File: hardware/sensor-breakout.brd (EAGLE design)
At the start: 44 x 44 mm, 67 parts, among them IC1 ATMEGA168-MU, U1 MCP73831, U2 NRF24L01SMD, U4 MCP5301, Y1 16M, Y2 12MHz

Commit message: hw: rc1
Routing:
- net GND: vias 38 -> 58
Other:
- board text added: "+3V3"
- board text added: "GND"
- board text added: "PC0"
- board text added: "PC1"
- board text added: "PC2"
- board text added: "PC3"
- board text added: "PD0"
- board text added: "PD3"
- board text added: "PD4"
- board text added: "SCL"
- board text added: "SDA"
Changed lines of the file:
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@@
 <rectangle x1="41.275" y1="1.905" x2="42.545" y2="3.175" layer="30"/>
 <rectangle x1="38.735" y1="1.905" x2="40.005" y2="3.175" layer="30"/>
+<text x="22.7584" y="5.08" size="0.6096" layer="121" rot="R90" align="center">PC0</text>
+<text x="22.7584" y="2.6416" size="0.6096" layer="121" rot="R90" align="center">+3V3</text>
+<text x="22.7584" y="7.7216" size="0.6096" layer="121" rot="R90" align="center">PC1</text>
+<text x="22.7584" y="10.16" size="0.6096" layer="121" rot="R90" align="center">PC2</text>
+<text x="22.7584" y="12.5984" size="0.6096" layer="121" rot="R90" align="center">PC3</text>
+<text x="22.7584" y="15.24" size="0.6096" layer="121" rot="R90" align="center">SDA</text>
+<text x="22.7584" y="17.8816" size="0.6096" layer="121" rot="R90" align="center">SCL</text>
+<text x="22.7584" y="20.32" size="0.6096" layer="121" rot="R90" align="center">PD0</text>
+<text x="22.7584" y="22.9616" size="0.6096" layer="121" rot="R90" align="center">PD3</text>
+<text x="22.7584" y="25.4" size="0.6096" layer="121" rot="R90" align="center">PD4</text>
+<text x="22.7584" y="35.56" size="0.6096" layer="121" rot="R90" align="center">GND</text>
 </plain>
 <attributes>
@@
 <via x="21.1328" y="0.8128" extent="1-16" drill="0.381"/>
 <wire x1="16.4592" y1="11.3792" x2="16.4592" y2="12.192" width="0" layer="19" extent="1-1"/>
+<via x="8.9408" y="7.9248" extent="1-16" drill="0.381"/>
+<via x="8.128" y="7.9248" extent="1-16" drill="0.381"/>
+<via x="8.3312" y="0.8128" extent="1-16" drill="0.381"/>
+<via x="18.0848" y="6.096" extent="1-16" drill="0.381"/>
+<via x="12.192" y="7.5184" extent="1-16" drill="0.381"/>
+<via x="14.8336" y="7.5184" extent="1-16" drill="0.381"/>
+<via x="0.8128" y="14.6304" extent="1-16" drill="0.381"/>
+<via x="4.064" y="15.6464" extent="1-16" drill="0.381"/>
+<via x="3.8608" y="26.8224" extent="1-16" drill="0.381"/>
+<via x="5.2832" y="26.8224" extent="1-16" drill="0.381"/>
+<via x="3.8608" y="24.5872" extent="1-16" drill="0.381"/>
+<via x="5.2832" y="24.5872" extent="1-16" drill="0.381"/>
+<via x="6.096" y="25.6032" extent="1-16" drill="0.381"/>
+<via x="15.24" y="23.368" extent="1-16" drill="0.381"/>
+<via x="19.9136" y="20.5232" extent="1-16" drill="0.381"/>
+<via x="19.5072" y="18.288" extent="1-16" drill="0.381"/>
+<via x="20.7264" y="17.0688" extent="1-16" drill="0.381"/>
+<via x="9.144" y="18.288" extent="1-16" drill="0.381"/>
+<via x="6.096" y="15.8496" extent="1-16" drill="0.381"/>
+<via x="8.128" y="16.8656" extent="1-16" drill="0.381"/>
 </signal>
 <signal name="+5V">
@@
 <via x="15.24" y="15.6464" extent="1-16" drill="0.381"/>
 <wire x1="15.24" y1="15.6464" x2="14.0208" y2="14.4272" width="0.2032" layer="16"/>
-<wire x1="14.0208" y1="14.4272" x2="14.0208" y2="10.9728" width="0.2032" layer="16"/>
-<wire x1="14.0208" y1="10.9728" x2="15.6464" y2="9.3472" width="0.2032" layer="16"/>
-<wire x1="15.6464" y1="9.3472" x2="15.6464" y2="6.9088" width="0.2032" layer="16"/>
+<wire x1="14.0208" y1="14.4272" x2="14.0208" y2="10.3632" width="0.2032" layer="16"/>
+<wire x1="14.0208" y1="10.3632" x2="15.6464" y2="8.7376" width="0.2032" layer="16"/>
+<wire x1="15.6464" y1="8.7376" x2="15.6464" y2="6.9088" width="0.2032" layer="16"/>
 <wire x1="15.6464" y1="6.9088" x2="17.4752" y2="5.08" width="0.2032" layer="16"/>
 <via x="17.4752" y="5.08" extent="1-16" drill="0.381"/>

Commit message: hw: rc2
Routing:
- net GND: vias 58 -> 59
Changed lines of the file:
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@@
 <setting verticaltext="up"/>
 </settings>
-<grid distance="8" unitdist="mil" unit="mil" style="lines" multiple="1" display="yes" altdistance="5" altunitdist="mil" altunit="mil"/>
+<grid distance="25" unitdist="mil" unit="mil" style="lines" multiple="1" display="yes" altdistance="5" altunitdist="mil" altunit="mil"/>
 <layers>
 <layer number="1" name="Top" color="4" fill="1" visible="yes" active="yes"/>
@@
 <text x="22.7584" y="25.4" size="0.6096" layer="121" rot="R90" align="center">PD4</text>
 <text x="22.7584" y="35.56" size="0.6096" layer="121" rot="R90" align="center">GND</text>
+<rectangle x1="36.195" y1="34.925" x2="37.465" y2="36.195" layer="29"/>
+<rectangle x1="38.735" y1="34.925" x2="40.005" y2="36.195" layer="29"/>
+<rectangle x1="41.275" y1="34.925" x2="42.545" y2="36.195" layer="29"/>
+<rectangle x1="36.195" y1="34.925" x2="37.465" y2="36.195" layer="30"/>
+<rectangle x1="38.735" y1="34.925" x2="40.005" y2="36.195" layer="30"/>
+<rectangle x1="41.275" y1="34.925" x2="42.545" y2="36.195" layer="30"/>
 </plain>
 <attributes>
@@
 <via x="31.75" y="35.56" extent="1-16" drill="1.016" diameter="1.8796"/>
 <via x="34.29" y="35.56" extent="1-16" drill="1.016" diameter="1.8796"/>
-<via x="36.83" y="35.56" extent="1-16" drill="1.016" diameter="1.8796"/>
-<via x="39.37" y="35.56" extent="1-16" drill="1.016" diameter="1.8796"/>
 <wire x1="20.7636" y1="15.8496" x2="20.7636" y2="15.406" width="0.6096" layer="1"/>
 <wire x1="20.7636" y1="15.406" x2="20.9296" y2="15.24" width="0.6096" layer="1"/>
 <wire x1="20.9296" y1="15.24" x2="20.9296" y2="14.6676" width="0.6096" layer="1"/>
 <wire x1="20.9296" y1="14.6676" x2="20.9668" y2="14.6304" width="0.6096" layer="1"/>
-<via x="41.91" y="35.56" extent="1-16" drill="1.016" diameter="1.8796"/>
 <via x="21.1328" y="0.8128" extent="1-16" drill="0.381"/>
-<wire x1="16.4592" y1="11.3792" x2="16.4592" y2="12.192" width="0" layer="19" extent="1-1"/>
 <via x="8.9408" y="7.9248" extent="1-16" drill="0.381"/>
 <via x="8.128" y="7.9248" extent="1-16" drill="0.381"/>
@@
 <via x="6.096" y="15.8496" extent="1-16" drill="0.381"/>
 <via x="8.128" y="16.8656" extent="1-16" drill="0.381"/>
+<via x="38.1" y="36.195" extent="1-16" drill="0.381"/>
+<via x="40.64" y="36.195" extent="1-16" drill="0.381"/>
+<via x="43.18" y="36.195" extent="1-16" drill="0.381"/>
+<via x="43.18" y="34.925" extent="1-16" drill="0.381"/>
+<wire x1="16.4592" y1="11.3792" x2="16.4592" y2="12.192" width="0" layer="19" extent="1-1"/>
 </signal>
 <signal name="+5V">

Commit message: hw: update values
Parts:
- R1: value TBD -> 3k9
- R2: value 2k2 -> 1k5
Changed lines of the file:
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@@
 <element name="C8" library="rcl" package="C0603" value="33p" x="18.288" y="20.32" rot="MR90"/>
 <element name="C9" library="rcl" package="C0603" value="33p" x="16.8656" y="20.32" rot="MR90"/>
-<element name="R2" library="rcl" package="R0603" value="2k2" x="7.3152" y="20.5232"/>
+<element name="R2" library="rcl" package="R0603" value="1k5" x="7.3152" y="20.5232"/>
 <element name="R3" library="rcl" package="R0603" value="68" x="6.2992" y="18.8976" rot="MR90"/>
 <element name="R4" library="rcl" package="R0603" value="68" x="7.7216" y="18.8976" rot="MR90"/>
@@
 <attribute name="PROD_ID" value="IC-09995" x="2.4384" y="12.5984" size="1.778" layer="27" rot="R270" display="off"/>
 </element>
-<element name="R1" library="rcl" package="R0603" value="TBD" x="3.6576" y="12.5984" rot="MR270"/>
+<element name="R1" library="rcl" package="R0603" value="3k9" x="3.6576" y="12.5984" rot="MR270"/>
 <element name="R5" library="rcl" package="R0603" value="5k6" x="7.9248" y="3.2512" rot="R270"/>
 <element name="R6" library="rcl" package="R0603" value="5k6" x="21.7424" y="3.8608" rot="R90"/>

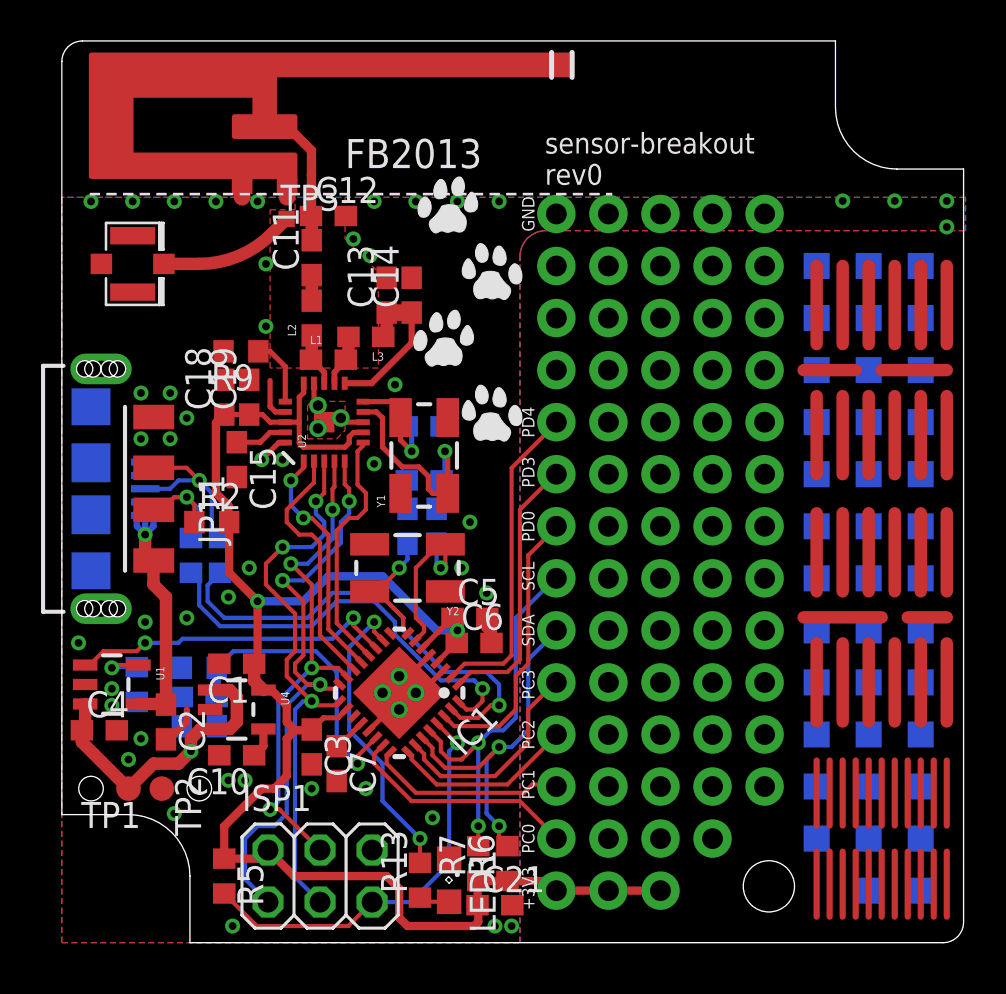
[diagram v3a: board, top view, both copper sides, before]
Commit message: hw: rev1, moved battery pads on bottom
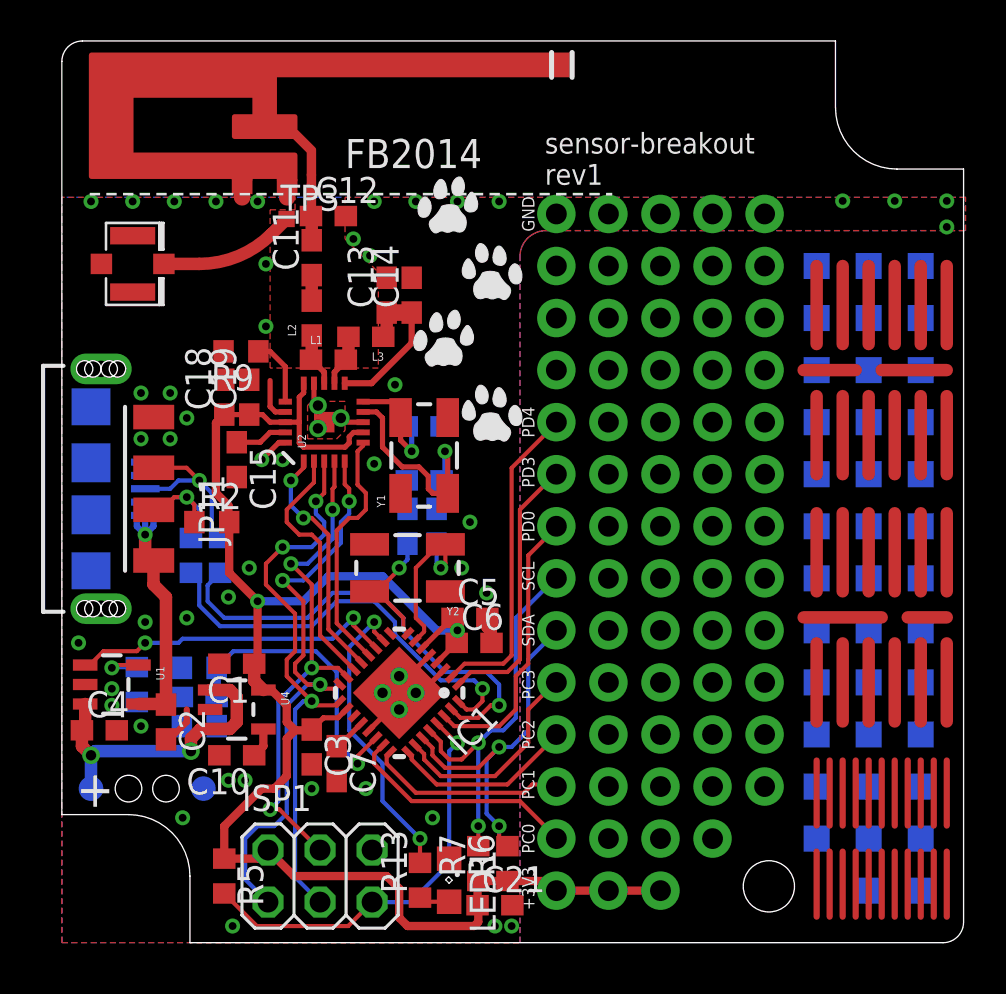
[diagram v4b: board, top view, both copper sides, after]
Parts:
- moved TP2 2.03 mm to (6.91, 7.52), flipped to the bottom
- moved TP1 1.83 mm to (1.42, 7.52), flipped to the bottom
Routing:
- net VBATT: track 16.2 -> 16.6 mm, vias 1 -> 2
- net GND: vias 59 -> 58
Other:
- board text added: "+"
- board text added: "FB2014"
- board text added: "sensor-breakout rev1"
- board text removed: "FB2013"
- board text removed: "sensor-breakout rev0"
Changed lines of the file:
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@@
 <setting verticaltext="up"/>
 </settings>
-<grid distance="25" unitdist="mil" unit="mil" style="lines" multiple="1" display="yes" altdistance="5" altunitdist="mil" altunit="mil"/>
+<grid distance="8" unitdist="mil" unit="mil" style="lines" multiple="1" display="yes" altdistance="5" altunitdist="mil" altunit="mil"/>
 <layers>
 <layer number="1" name="Top" color="4" fill="1" visible="yes" active="yes"/>
@@
 <board>
 <plain>
-<hole x="6.7056" y="7.5184" drill="1.2"/>
-<hole x="1.4224" y="7.5184" drill="1.2"/>
-<text x="13.8176" y="37.7952" size="1.4224" layer="121">FB2013</text>
+<hole x="5.08" y="7.5184" drill="1.3"/>
+<hole x="3.2512" y="7.5184" drill="1.3"/>
+<text x="13.8176" y="37.7952" size="1.4224" layer="121">FB2014</text>
 <text x="23.5712" y="36.9824" size="1.016" layer="121">sensor-breakout
-rev0</text>
+rev1</text>
 <rectangle x1="11.9888" y1="24.6888" x2="13.6144" y2="26.3144" layer="29"/>
 <wire x1="-5" y1="22" x2="49" y2="22" width="0.4064" layer="47"/>
@@
 <rectangle x1="38.735" y1="34.925" x2="40.005" y2="36.195" layer="30"/>
 <rectangle x1="41.275" y1="34.925" x2="42.545" y2="36.195" layer="30"/>
+<text x="1.6256" y="7.5184" size="1.778" layer="121" align="center">+</text>
 </plain>
 <attributes>
@@
 </element>
 <element name="U$1" library="antenna" package="DN007-2" value="INVERTED_F_ANTENNA-2" x="9.9568" y="39.8272"/>
-<element name="TP1" library="testpad" package="TP12R" value="TPTP12R" x="3.2512" y="7.5184" rot="R180">
-<attribute name="TP_SIGNAL_NAME" value="" x="-13.2588" y="63.3984" size="1.778" layer="27" rot="R180" display="off"/>
+<element name="TP1" library="testpad" package="TP12R" value="TPTP12R" x="1.4224" y="7.5184" rot="MR180">
+<attribute name="TP_SIGNAL_NAME" value="" x="17.9324" y="63.3984" size="1.778" layer="28" rot="MR180" display="off"/>
 </element>
-<element name="TP2" library="testpad" package="TP12R" value="TPTP12R" x="4.8768" y="7.5184" rot="R270">
-<attribute name="TP_SIGNAL_NAME" value="" x="-51.0032" y="-14.0716" size="1.778" layer="27" rot="R270" display="off"/>
+<element name="TP2" library="testpad" package="TP12R" value="TPTP12R" x="6.9088" y="7.5184" rot="MR270">
+<attribute name="TP_SIGNAL_NAME" value="" x="62.7888" y="-14.0716" size="1.778" layer="28" rot="MR270" display="off"/>
 </element>
 <element name="U$2" library="SparkFun-Connectors" package="U.FL" value="U.FL" x="3.4544" y="33.1216"/>
@@
 <via x="2.4384" y="12.3952" extent="1-16" drill="0.381"/>
 <via x="2.4384" y="11.5824" extent="1-16" drill="0.381"/>
-<via x="3.2512" y="8.9408" extent="1-16" drill="0.381"/>
-<via x="3.8608" y="9.9568" extent="1-16" drill="0.381"/>
+<via x="3.8608" y="10.5664" extent="1-16" drill="0.381"/>
 <wire x1="14.974275" y1="10.353521875" x2="15.999953125" y2="11.3792" width="0.254" layer="1"/>
 <wire x1="15.999953125" y1="11.3792" x2="16.4592" y2="11.3792" width="0.254" layer="1"/>
@@
 <wire x1="6.096" y1="10.7696" x2="5.2832" y2="9.9568" width="0.3048" layer="1"/>
 <wire x1="5.2832" y1="9.9568" x2="4.8768" y2="9.9568" width="0.3048" layer="1"/>
-<via x="5.4864" y="6.2992" extent="1-16" drill="0.381"/>
+<via x="5.8928" y="6.096" extent="1-16" drill="0.381"/>
 <via x="10.7696" y="23.5712" extent="1-16" drill="0.381"/>
 <via x="9.7536" y="23.5712" extent="1-16" drill="0.381"/>
@@
 <wire x1="1.1383" y1="11.6484" x2="1.1383" y2="10.5227" width="0.6096" layer="1"/>
 <wire x1="1.1383" y1="10.5227" x2="0.9788" y2="10.3632" width="0.6096" layer="1"/>
-<wire x1="0.9788" y1="10.3632" x2="0.9788" y2="9.7908" width="0.6096" layer="1"/>
-<wire x1="0.9788" y1="9.7908" x2="3.2512" y2="7.5184" width="0.6096" layer="1"/>
-<wire x1="3.2512" y1="7.5184" x2="4.4704" y2="8.7376" width="0.6096" layer="1"/>
-<wire x1="4.4704" y1="8.7376" x2="5.6896" y2="8.7376" width="0.6096" layer="1"/>
-<wire x1="5.6896" y1="8.7376" x2="6.2992" y2="9.3472" width="0.6096" layer="1"/>
 <wire x1="6.2992" y1="9.9568" x2="6.7716" y2="10.4292" width="0.6096" layer="1"/>
 <wire x1="7.2343" y1="10.4292" x2="6.7716" y2="10.4292" width="0.6096" layer="1"/>
@@
 <wire x1="8.194" y1="12.3292" x2="8.5344" y2="11.9888" width="0.6096" layer="1"/>
 <wire x1="6.2992" y1="9.3472" x2="6.2992" y2="9.9568" width="0.6096" layer="1"/>
-<via x="6.2992" y="9.3472" extent="1-16" drill="0.381"/>
+<via x="6.2992" y="9.3472" extent="1-16" drill="0.508"/>
 <wire x1="6.2992" y1="9.3472" x2="6.2992" y2="10.1228" width="0.4064" layer="16"/>
 <wire x1="6.2992" y1="10.1228" x2="5.8556" y2="10.5664" width="0.4064" layer="16"/>
+<wire x1="0.9788" y1="10.3632" x2="0.9788" y2="9.5876" width="0.6096" layer="1"/>
+<wire x1="0.9788" y1="9.5876" x2="1.4224" y2="9.144" width="0.6096" layer="1"/>
+<via x="1.4224" y="9.144" extent="1-16" drill="0.508"/>
+<wire x1="1.4224" y1="9.144" x2="1.4224" y2="7.5184" width="0.6096" layer="16"/>
+<wire x1="1.4224" y1="9.144" x2="1.6256" y2="9.3472" width="0.6096" layer="16"/>
+<wire x1="1.6256" y1="9.3472" x2="6.2992" y2="9.3472" width="0.6096" layer="16"/>
 </signal>
 <signal name="+3V3">

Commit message: hw: fix ldo part number
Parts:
- U4: value MCP5301 -> MIC5301
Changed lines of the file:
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@@
 <element name="C1" library="rcl" package="C0603" value=".1u" x="8.5344" y="13.6144" rot="R180"/>
 <element name="C2" library="rcl" package="C0603" value=".1u" x="5.08" y="10.7696" rot="R270"/>
-<element name="U4" library="SparkFun-PowerIC" package="SOT23-5" value="MCP5301" x="8.5344" y="11.3792" rot="R270"/>
+<element name="U4" library="SparkFun-PowerIC" package="SOT23-5" value="MIC5301" x="8.5344" y="11.3792" rot="R270"/>
 <element name="C4" library="rcl" package="C0603" value="1u" x="1.8288" y="10.3632"/>
 <element name="IC1" library="balto" package="MLF32-TH" value="ATMEGA168-MU" x="16.4592" y="12.192" rot="R225"/>
